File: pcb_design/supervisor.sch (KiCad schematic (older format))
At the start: 17 parts, among them U5 7400-TSSOP, U6 SN74ALVC08PWR, U7 SN74ALVC08PWR, U8 SN74AUP1G74

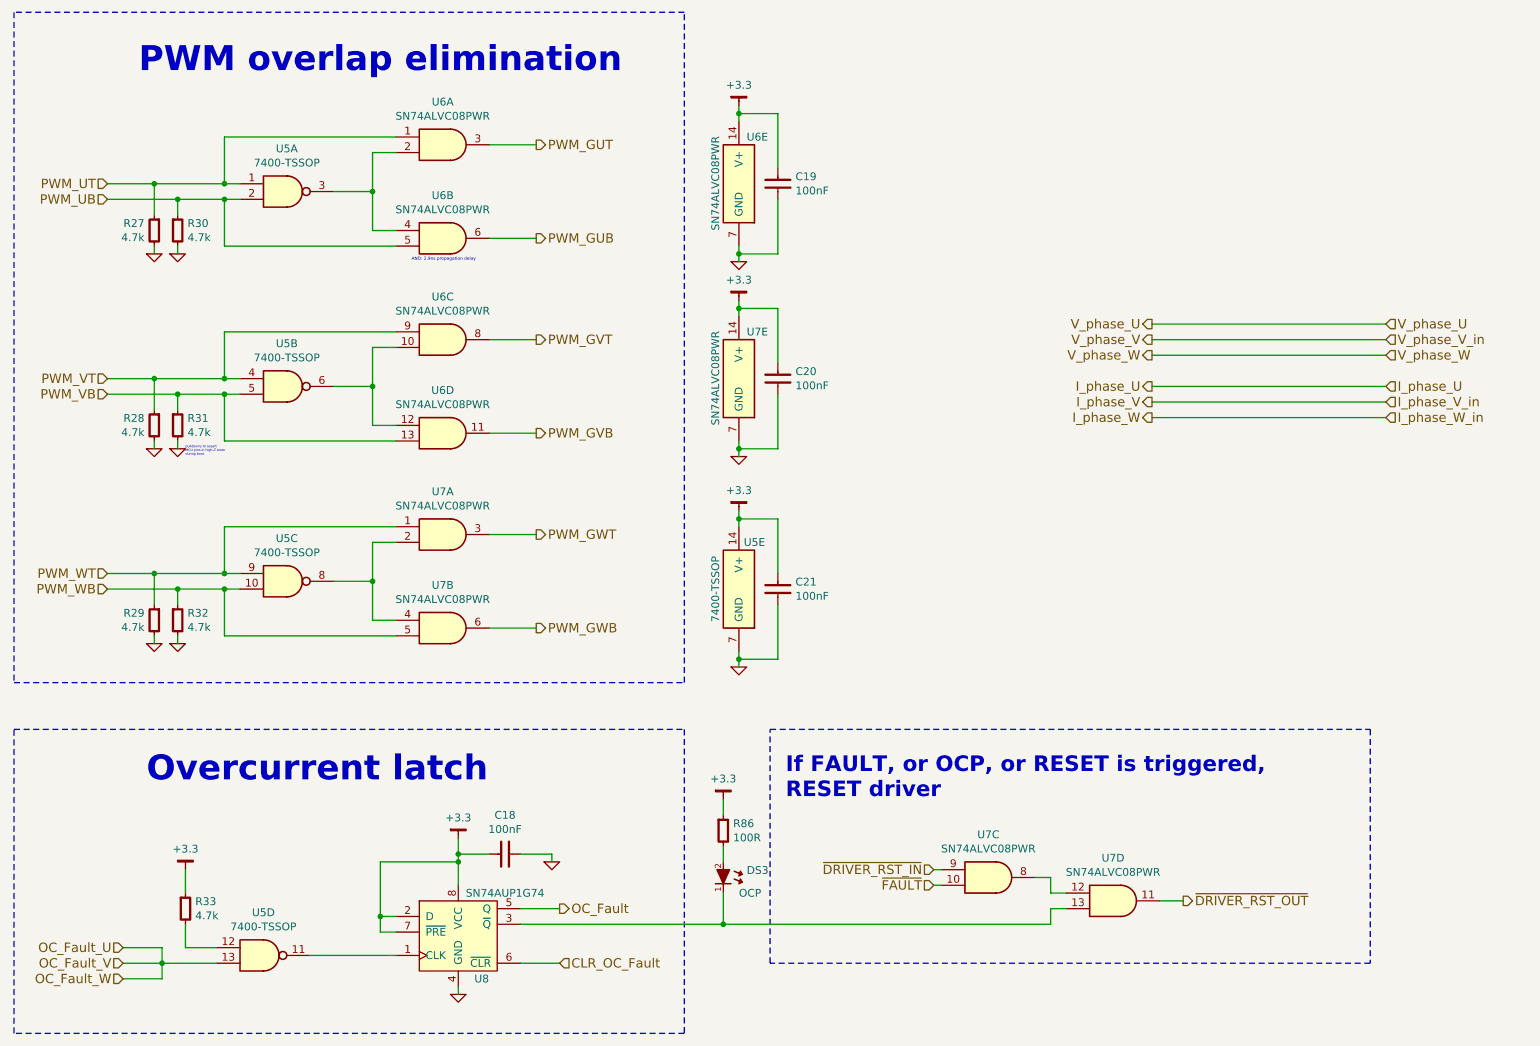
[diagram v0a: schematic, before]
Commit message: Added reverse polarity protection on the isolated side of CON connector. Also, more layout
Signed-off-by: Marcos Chaparro <mchaparro@paltatech.com>
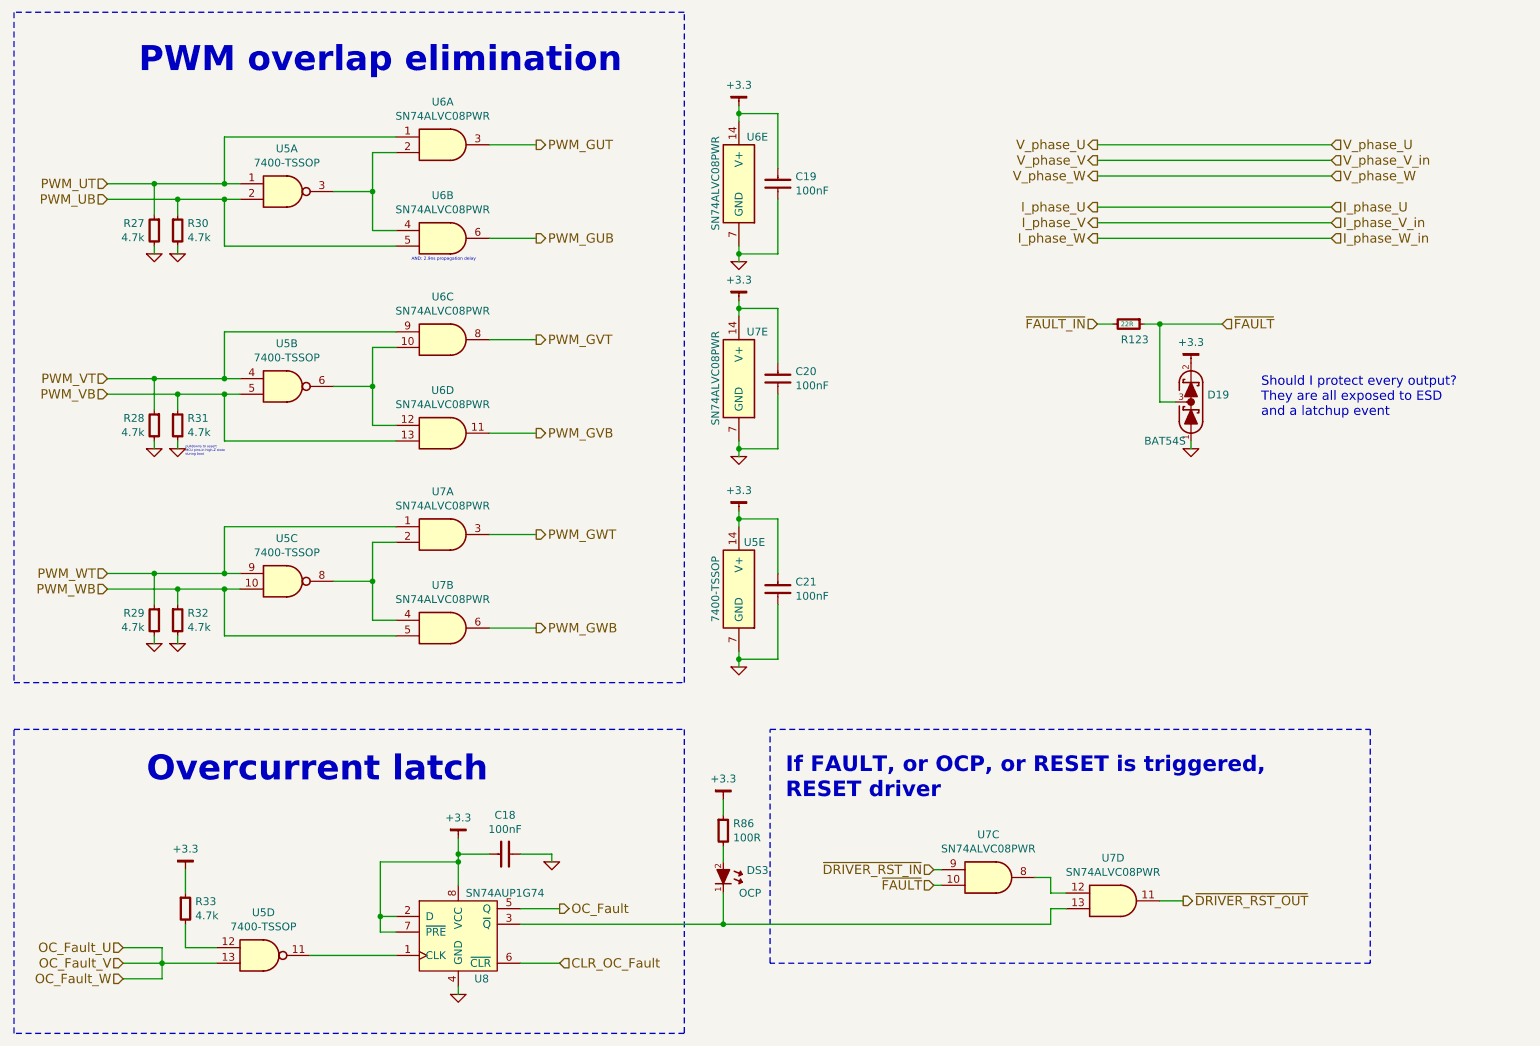
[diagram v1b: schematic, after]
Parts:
- added D19: BAT54S, smd-semi:SOT-23, symbol BAT54S
- added R123: 22R, IPC7351-Nominal:RESC1608X50, symbol R-0603
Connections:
- net +3.3: now also D19.2 (K)
- net GND: now also D19.1 (A)
- net ~FAULT: now also D19.3 (COM), R123.1
- new net ~FAULT_IN: R123.2
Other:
- note added: "Should I protect every output?\nThey are all exposed to ESD \nand a latchup event"
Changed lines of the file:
@@
 Text HLabel 6850 6450 0    60   Input ~ 0
 ~FAULT
-Text HLabel 9750 2850 2    60   Input ~ 0
+Text HLabel 9400 1700 2    60   Input ~ 0
 V_phase_U
-Text HLabel 8250 2850 0    60   Output ~ 0
+Text HLabel 7900 1700 0    60   Output ~ 0
 V_phase_U
-Text HLabel 9750 2950 2    60   Input ~ 0
+Text HLabel 9400 1800 2    60   Input ~ 0
 V_phase_V_in
-Text HLabel 9750 3050 2    60   Input ~ 0
+Text HLabel 9400 1900 2    60   Input ~ 0
 V_phase_W
-Text HLabel 8250 2950 0    60   Output ~ 0
+Text HLabel 7900 1800 0    60   Output ~ 0
 V_phase_V
-Text HLabel 8250 3050 0    60   Output ~ 0
+Text HLabel 7900 1900 0    60   Output ~ 0
 V_phase_W
 Wire Wire Line
-	9750 2850 8250 2850
-Wire Wire Line
-	9750 2950 8250 2950
-Wire Wire Line
-	8250 3050 9750 3050
-Text HLabel 9750 3250 2    60   Input ~ 0
+	9400 1700 7900 1700
+Wire Wire Line
+	9400 1800 7900 1800
+Wire Wire Line
+	7900 1900 9400 1900
+Text HLabel 9400 2100 2    60   Input ~ 0
 I_phase_U
-Text HLabel 8250 3250 0    60   Output ~ 0
+Text HLabel 7900 2100 0    60   Output ~ 0
 I_phase_U
-Text HLabel 9750 3350 2    60   Input ~ 0
+Text HLabel 9400 2200 2    60   Input ~ 0
 I_phase_V_in
-Text HLabel 9750 3450 2    60   Input ~ 0
+Text HLabel 9400 2300 2    60   Input ~ 0
 I_phase_W_in
-Text HLabel 8250 3350 0    60   Output ~ 0
+Text HLabel 7900 2200 0    60   Output ~ 0
 I_phase_V
-Text HLabel 8250 3450 0    60   Output ~ 0
+Text HLabel 7900 2300 0    60   Output ~ 0
 I_phase_W
 Wire Wire Line
-	9750 3250 8250 3250
-Wire Wire Line
-	9750 3350 8250 3350
-Wire Wire Line
-	8250 3450 9750 3450
+	9400 2100 7900 2100
+Wire Wire Line
+	9400 2200 7900 2200
+Wire Wire Line
+	7900 2300 9400 2300
 Wire Wire Line
 	3250 2250 3400 2250
@@
 	3400 2350 2300 2350
 Wire Wire Line
-	2300 2350 2300 2050
+	2300 2050 2300 2350
 Wire Wire Line
 	1550 2050 2400 2050
@@
 Connection ~ 2000 2050
 $Comp
-L GND #PWR086
+L GND #PWR88
 U 1 1 588831C2
 P 1850 2400
-F 0 "#PWR086" H 1850 2400 30  0001 C CNN
+F 0 "#PWR88" H 1850 2400 30  0001 C CNN
 F 1 "GND" H 1850 2330 30  0001 C CNN
 F 2 "" H 1850 2400 60  0000 C CNN
@@
 	1850 2400 1850 2350
 $Comp
-L GND #PWR087
+L GND #PWR91
 U 1 1 58883201
 P 2000 2400
-F 0 "#PWR087" H 2000 2400 30  0001 C CNN
+F 0 "#PWR91" H 2000 2400 30  0001 C CNN
 F 1 "GND" H 2000 2330 30  0001 C CNN
 F 2 "" H 2000 2400 60  0000 C CNN
@@
 	3400 3600 2300 3600
 Wire Wire Line
-	2300 3600 2300 3300
+	2300 3300 2300 3600
 Wire Wire Line
 	1550 3300 2400 3300
@@
 Connection ~ 2000 3300
 $Comp
-L GND #PWR088
+L GND #PWR89
 U 1 1 588824FD
 P 1850 3650
-F 0 "#PWR088" H 1850 3650 30  0001 C CNN
+F 0 "#PWR89" H 1850 3650 30  0001 C CNN
 F 1 "GND" H 1850 3580 30  0001 C CNN
 F 2 "" H 1850 3650 60  0000 C CNN
@@
 	1850 3650 1850 3600
 $Comp
-L GND #PWR089
+L GND #PWR92
 U 1 1 58882504
 P 2000 3650
-F 0 "#PWR089" H 2000 3650 30  0001 C CNN
+F 0 "#PWR92" H 2000 3650 30  0001 C CNN
 F 1 "GND" H 2000 3580 30  0001 C CNN
 F 2 "" H 2000 3650 60  0000 C CNN
@@
 	3400 4850 2300 4850
 Wire Wire Line
-	2300 4850 2300 4550
+	2300 4550 2300 4850
 Wire Wire Line
 	1550 4550 2400 4550
@@
 Connection ~ 2000 4550
 $Comp
-L GND #PWR090
+L GND #PWR90
 U 1 1 5888288C
 P 1850 4900
-F 0 "#PWR090" H 1850 4900 30  0001 C CNN
+F 0 "#PWR90" H 1850 4900 30  0001 C CNN
 F 1 "GND" H 1850 4830 30  0001 C CNN
 F 2 "" H 1850 4900 60  0000 C CNN
@@
 	1850 4900 1850 4850
 $Comp
-L GND #PWR091
+L GND #PWR93
 U 1 1 58882893
 P 2000 4900
-F 0 "#PWR091" H 2000 4900 30  0001 C CNN
+F 0 "#PWR93" H 2000 4900 30  0001 C CNN
 F 1 "GND" H 2000 4830 30  0001 C CNN
 F 2 "" H 2000 4900 60  0000 C CNN
@@
 $EndComp
 $Comp
-L GND #PWR092
+L GND #PWR96
 U 1 1 5888A11E
 P 3800 7150
-F 0 "#PWR092" H 3800 7150 30  0001 C CNN
+F 0 "#PWR96" H 3800 7150 30  0001 C CNN
 F 1 "GND" H 3800 7080 30  0001 C CNN
 F 2 "" H 3800 7150 60  0000 C CNN
@@
 	4400 6250 4400 6300
 $Comp
-L GND #PWR093
+L GND #PWR97
 U 1 1 5888A46C
 P 4400 6300
-F 0 "#PWR093" H 4400 6300 30  0001 C CNN
+F 0 "#PWR97" H 4400 6300 30  0001 C CNN
 F 1 "GND" H 4400 6230 30  0001 C CNN
 F 2 "" H 4400 6300 60  0000 C CNN
@@
 	5600 4950 5600 5050
 $Comp
-L GND #PWR094
+L GND #PWR104
 U 1 1 58899228
 P 5600 5050
-F 0 "#PWR094" H 5600 5050 30  0001 C CNN
+F 0 "#PWR104" H 5600 5050 30  0001 C CNN
 F 1 "GND" H 5600 4980 30  0001 C CNN
 F 2 "" H 5600 5050 60  0000 C CNN
@@
 Connection ~ 5600 5000
 $Comp
-L GND #PWR095
+L GND #PWR102
 U 1 1 5889937C
 P 5600 3700
-F 0 "#PWR095" H 5600 3700 30  0001 C CNN
+F 0 "#PWR102" H 5600 3700 30  0001 C CNN
 F 1 "GND" H 5600 3630 30  0001 C CNN
 F 2 "" H 5600 3700 60  0000 C CNN
@@
 $EndComp
 $Comp
-L GND #PWR096
+L GND #PWR100
 U 1 1 588993D2
 P 5600 2450
-F 0 "#PWR096" H 5600 2450 30  0001 C CNN
+F 0 "#PWR100" H 5600 2450 30  0001 C CNN
 F 1 "GND" H 5600 2380 30  0001 C CNN
 F 2 "" H 5600 2450 60  0000 C CNN
@@
 $EndComp
 Wire Wire Line
-	5600 2450 5600 2350
+	5600 2350 5600 2450
 Wire Wire Line
 	5850 4450 5850 4100
@@
 Connection ~ 5600 4100
 Wire Wire Line
-	5600 3700 5600 3600
+	5600 3600 5600 3700
 $Comp
 L C-0603 C20
@@
 	5500 5900 5500 6000
 $Comp
-L +3.3 #PWR097
+L +3.3 #PWR103
 U 1 1 588B453A
 P 5600 4050
-F 0 "#PWR097" H 5650 4100 30  0001 C CNN
+F 0 "#PWR103" H 5650 4100 30  0001 C CNN
 F 1 "+3.3" H 5600 4183 50  0000 C CNN
 F 2 "" H -950 100 60  0000 C CNN
@@
 $EndComp
 $Comp
-L +3.3 #PWR098
+L +3.3 #PWR101
 U 1 1 588B46D1
 P 5600 2700
-F 0 "#PWR098" H 5650 2750 30  0001 C CNN
+F 0 "#PWR101" H 5650 2750 30  0001 C CNN
 F 1 "+3.3" H 5600 2833 50  0000 C CNN
 F 2 "" H -950 -1250 60  0000 C CNN
@@
 $EndComp
 $Comp
-L +3.3 #PWR099
+L +3.3 #PWR99
 U 1 1 588B47E2
 P 5600 1450
-F 0 "#PWR099" H 5650 1500 30  0001 C CNN
+F 0 "#PWR99" H 5650 1500 30  0001 C CNN
 F 1 "+3.3" H 5600 1583 50  0000 C CNN
 F 2 "" H -950 -2500 60  0000 C CNN
@@
 $EndComp
 $Comp
-L +3.3 #PWR0100
+L +3.3 #PWR98
 U 1 1 588B4A14
 P 5500 5900
-F 0 "#PWR0100" H 5550 5950 30  0001 C CNN
+F 0 "#PWR98" H 5550 5950 30  0001 C CNN
 F 1 "+3.3" H 5500 6033 50  0000 C CNN
 F 2 "" H -1050 1950 60  0000 C CNN
@@
 $EndComp
 $Comp
-L +3.3 #PWR0101
+L +3.3 #PWR95
 U 1 1 588B4BFB
 P 3800 6150
-F 0 "#PWR0101" H 3850 6200 30  0001 C CNN
+F 0 "#PWR95" H 3850 6200 30  0001 C CNN
 F 1 "+3.3" H 3800 6283 50  0000 C CNN
 F 2 "" H -2750 2200 60  0000 C CNN
@@
 $EndComp
 $Comp
-L +3.3 #PWR0102
+L +3.3 #PWR94
 U 1 1 588B4CB5
 P 2050 6350
-F 0 "#PWR0102" H 2100 6400 30  0001 C CNN
+F 0 "#PWR94" H 2100 6400 30  0001 C CNN
 F 1 "+3.3" H 2050 6483 50  0000 C CNN
 F 2 "" H -4500 2400 60  0000 C CNN
@@
 Text Notes 2050 3700 0    15   ~ 0
 pulldowns to assert\nMCU pins in high-Z state\nduring boot
+Text HLabel 7900 2850 0    60   Input ~ 0
+~FAULT_IN
+$Comp
+L R-0603 R123
+U 1 1 589012E3
+P 8100 2850
+F 0 "R123" V 8200 2800 50  0000 L CNN
+F 1 "22R" V 8100 2800 30  0000 L CNN
+F 2 "IPC7351-Nominal:RESC1608X50" H 8100 2850 50  0001 C CNN
+F 3 "" H 8100 2900 60  0000 C CNN
+F 4 "RES SMD 1k 5% [0603]" H 8850 3400 60  0001 C CNN "BOM"
+	1    8100 2850
+	0    1    1    0
+$EndComp
+Wire Wire Line
+	8000 2850 7900 2850
+$Comp
+L BAT54S D19
+U 1 1 589036F3
+P 8500 3350
+F 0 "D19" V 8546 3245 50  0000 R CNN
+F 1 "BAT54S" V 8250 3650 50  0000 R CNN
+F 2 "smd-semi:SOT-23" H 8500 3200 60  0001 C CNN
+F 3 "" V 8450 3350 60  0000 C CNN
+F 4 "SCHOTTKY BAT54S" H 8500 3100 60  0001 C CNN "BOM"
+	1    8500 3350
+	0    -1   -1   0
+$EndComp
+$Comp
+L GND #PWR?
+U 1 1 589036FA
+P 8500 3650
+AR Path="/5886DA84/589036FA" Ref="#PWR?"  Part="1"
+AR Path="/588C2790/589036FA" Ref="#PWR?"  Part="1"
+AR Path="/588C4E84/589036FA" Ref="#PWR?"  Part="1"
+AR Path="/5888D059/589036FA" Ref="#PWR106"  Part="1"
+F 0 "#PWR106" H 8500 3650 30  0001 C CNN
+F 1 "GND" H 8500 3580 30  0001 C CNN
+F 2 "" H 8500 3650 60  0000 C CNN
+F 3 "" H 8500 3650 60  0000 C CNN
+	1    8500 3650
+	1    0    0    -1
+$EndComp
+$Comp
+L +3.3 #PWR?
+U 1 1 58903700
+P 8500 3100
+AR Path="/5886DA84/58903700" Ref="#PWR?"  Part="1"
+AR Path="/588C2790/58903700" Ref="#PWR?"  Part="1"
+AR Path="/588C4E84/58903700" Ref="#PWR?"  Part="1"
+AR Path="/5888D059/58903700" Ref="#PWR105"  Part="1"
+F 0 "#PWR105" H 8550 3150 30  0001 C CNN
+F 1 "+3.3" H 8500 3233 50  0000 C CNN
+F 2 "" H 650 -2000 60  0000 C CNN
+F 3 "" H 650 -2000 60  0000 C CNN
+	1    8500 3100
+	1    0    0    -1
+$EndComp
+Wire Wire Line
+	8500 3600 8500 3650
+Wire Wire Line
+	8200 2850 8700 2850
+Text HLabel 8700 2850 2    60   Input ~ 0
+~FAULT
+Wire Wire Line
+	8400 3350 8300 3350
+Wire Wire Line
+	8300 3350 8300 2850
+Connection ~ 8300 2850
+Text Notes 8950 3450 0    60   ~ 0
+Should I protect every output?\nThey are all exposed to ESD \nand a latchup event
 $EndSCHEMATC

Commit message: Resolver routed using push pull buffer
Signed-off-by: Marcos Chaparro <mchaparro@paltatech.com>
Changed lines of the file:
@@
 	3400 2350 2300 2350
 Wire Wire Line
-	2300 2050 2300 2350
+	2300 2350 2300 2050
 Wire Wire Line
 	1550 2050 2400 2050
@@
 Connection ~ 2000 2050
 $Comp
-L GND #PWR88
+L GND #PWR094
 U 1 1 588831C2
 P 1850 2400
-F 0 "#PWR88" H 1850 2400 30  0001 C CNN
+F 0 "#PWR094" H 1850 2400 30  0001 C CNN
 F 1 "GND" H 1850 2330 30  0001 C CNN
 F 2 "" H 1850 2400 60  0000 C CNN
@@
 	1850 2400 1850 2350
 $Comp
-L GND #PWR91
+L GND #PWR095
 U 1 1 58883201
 P 2000 2400
-F 0 "#PWR91" H 2000 2400 30  0001 C CNN
+F 0 "#PWR095" H 2000 2400 30  0001 C CNN
 F 1 "GND" H 2000 2330 30  0001 C CNN
 F 2 "" H 2000 2400 60  0000 C CNN
@@
 	3400 3600 2300 3600
 Wire Wire Line
-	2300 3300 2300 3600
+	2300 3600 2300 3300
 Wire Wire Line
 	1550 3300 2400 3300
@@
 Connection ~ 2000 3300
 $Comp
-L GND #PWR89
+L GND #PWR096
 U 1 1 588824FD
 P 1850 3650
-F 0 "#PWR89" H 1850 3650 30  0001 C CNN
+F 0 "#PWR096" H 1850 3650 30  0001 C CNN
 F 1 "GND" H 1850 3580 30  0001 C CNN
 F 2 "" H 1850 3650 60  0000 C CNN
@@
 	1850 3650 1850 3600
 $Comp
-L GND #PWR92
+L GND #PWR097
 U 1 1 58882504
 P 2000 3650
-F 0 "#PWR92" H 2000 3650 30  0001 C CNN
+F 0 "#PWR097" H 2000 3650 30  0001 C CNN
 F 1 "GND" H 2000 3580 30  0001 C CNN
 F 2 "" H 2000 3650 60  0000 C CNN
@@
 	3400 4850 2300 4850
 Wire Wire Line
-	2300 4550 2300 4850
+	2300 4850 2300 4550
 Wire Wire Line
 	1550 4550 2400 4550
@@
 Connection ~ 2000 4550
 $Comp
-L GND #PWR90
+L GND #PWR098
 U 1 1 5888288C
 P 1850 4900
-F 0 "#PWR90" H 1850 4900 30  0001 C CNN
+F 0 "#PWR098" H 1850 4900 30  0001 C CNN
 F 1 "GND" H 1850 4830 30  0001 C CNN
 F 2 "" H 1850 4900 60  0000 C CNN
@@
 	1850 4900 1850 4850
 $Comp
-L GND #PWR93
+L GND #PWR099
 U 1 1 58882893
 P 2000 4900
-F 0 "#PWR93" H 2000 4900 30  0001 C CNN
+F 0 "#PWR099" H 2000 4900 30  0001 C CNN
 F 1 "GND" H 2000 4830 30  0001 C CNN
 F 2 "" H 2000 4900 60  0000 C CNN
@@
 $EndComp
 $Comp
-L GND #PWR96
+L GND #PWR0100
 U 1 1 5888A11E
 P 3800 7150
-F 0 "#PWR96" H 3800 7150 30  0001 C CNN
+F 0 "#PWR0100" H 3800 7150 30  0001 C CNN
 F 1 "GND" H 3800 7080 30  0001 C CNN
 F 2 "" H 3800 7150 60  0000 C CNN
@@
 	4400 6250 4400 6300
 $Comp
-L GND #PWR97
+L GND #PWR0101
 U 1 1 5888A46C
 P 4400 6300
-F 0 "#PWR97" H 4400 6300 30  0001 C CNN
+F 0 "#PWR0101" H 4400 6300 30  0001 C CNN
 F 1 "GND" H 4400 6230 30  0001 C CNN
 F 2 "" H 4400 6300 60  0000 C CNN
@@
 	5600 4950 5600 5050
 $Comp
-L GND #PWR104
+L GND #PWR0102
 U 1 1 58899228
 P 5600 5050
-F 0 "#PWR104" H 5600 5050 30  0001 C CNN
+F 0 "#PWR0102" H 5600 5050 30  0001 C CNN
 F 1 "GND" H 5600 4980 30  0001 C CNN
 F 2 "" H 5600 5050 60  0000 C CNN
@@
 Connection ~ 5600 5000
 $Comp
-L GND #PWR102
+L GND #PWR0103
 U 1 1 5889937C
 P 5600 3700
-F 0 "#PWR102" H 5600 3700 30  0001 C CNN
+F 0 "#PWR0103" H 5600 3700 30  0001 C CNN
 F 1 "GND" H 5600 3630 30  0001 C CNN
 F 2 "" H 5600 3700 60  0000 C CNN
@@
 $EndComp
 $Comp
-L GND #PWR100
+L GND #PWR0104
 U 1 1 588993D2
 P 5600 2450
-F 0 "#PWR100" H 5600 2450 30  0001 C CNN
+F 0 "#PWR0104" H 5600 2450 30  0001 C CNN
 F 1 "GND" H 5600 2380 30  0001 C CNN
 F 2 "" H 5600 2450 60  0000 C CNN
@@
 	5500 5900 5500 6000
 $Comp
-L +3.3 #PWR103
+L +3.3 #PWR0105
 U 1 1 588B453A
 P 5600 4050
-F 0 "#PWR103" H 5650 4100 30  0001 C CNN
+F 0 "#PWR0105" H 5650 4100 30  0001 C CNN
 F 1 "+3.3" H 5600 4183 50  0000 C CNN
 F 2 "" H -950 100 60  0000 C CNN
@@
 $EndComp
 $Comp
-L +3.3 #PWR101
+L +3.3 #PWR0106
 U 1 1 588B46D1
 P 5600 2700
-F 0 "#PWR101" H 5650 2750 30  0001 C CNN
+F 0 "#PWR0106" H 5650 2750 30  0001 C CNN
 F 1 "+3.3" H 5600 2833 50  0000 C CNN
 F 2 "" H -950 -1250 60  0000 C CNN
@@
 $EndComp
 $Comp
-L +3.3 #PWR99
+L +3.3 #PWR0107
 U 1 1 588B47E2
 P 5600 1450
-F 0 "#PWR99" H 5650 1500 30  0001 C CNN
+F 0 "#PWR0107" H 5650 1500 30  0001 C CNN
 F 1 "+3.3" H 5600 1583 50  0000 C CNN
 F 2 "" H -950 -2500 60  0000 C CNN
@@
 $EndComp
 $Comp
-L +3.3 #PWR98
+L +3.3 #PWR0108
 U 1 1 588B4A14
 P 5500 5900
-F 0 "#PWR98" H 5550 5950 30  0001 C CNN
+F 0 "#PWR0108" H 5550 5950 30  0001 C CNN
 F 1 "+3.3" H 5500 6033 50  0000 C CNN
 F 2 "" H -1050 1950 60  0000 C CNN
@@
 $EndComp
 $Comp
-L +3.3 #PWR95
+L +3.3 #PWR0109
 U 1 1 588B4BFB
 P 3800 6150
-F 0 "#PWR95" H 3850 6200 30  0001 C CNN
+F 0 "#PWR0109" H 3850 6200 30  0001 C CNN
 F 1 "+3.3" H 3800 6283 50  0000 C CNN
 F 2 "" H -2750 2200 60  0000 C CNN
@@
 $EndComp
 $Comp
-L +3.3 #PWR94
+L +3.3 #PWR0110
 U 1 1 588B4CB5
 P 2050 6350
-F 0 "#PWR94" H 2100 6400 30  0001 C CNN
+F 0 "#PWR0110" H 2100 6400 30  0001 C CNN
 F 1 "+3.3" H 2050 6483 50  0000 C CNN
 F 2 "" H -4500 2400 60  0000 C CNN
@@
 AR Path="/588C2790/589036FA" Ref="#PWR?"  Part="1"
 AR Path="/588C4E84/589036FA" Ref="#PWR?"  Part="1"
-AR Path="/5888D059/589036FA" Ref="#PWR106"  Part="1"
-F 0 "#PWR106" H 8500 3650 30  0001 C CNN
+AR Path="/5888D059/589036FA" Ref="#PWR0111"  Part="1"
+F 0 "#PWR0111" H 8500 3650 30  0001 C CNN
 F 1 "GND" H 8500 3580 30  0001 C CNN
 F 2 "" H 8500 3650 60  0000 C CNN
@@
 AR Path="/588C2790/58903700" Ref="#PWR?"  Part="1"
 AR Path="/588C4E84/58903700" Ref="#PWR?"  Part="1"
-AR Path="/5888D059/58903700" Ref="#PWR105"  Part="1"
-F 0 "#PWR105" H 8550 3150 30  0001 C CNN
+AR Path="/5888D059/58903700" Ref="#PWR0112"  Part="1"
+F 0 "#PWR0112" H 8550 3150 30  0001 C CNN
 F 1 "+3.3" H 8500 3233 50  0000 C CNN
 F 2 "" H 650 -2000 60  0000 C CNN
